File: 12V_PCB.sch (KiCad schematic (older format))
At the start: 8 parts, among them J1 12V IN, J2 RPI CONN, J3 BTN CONN, J4 LED CONN, Q1 PMV40UN2R

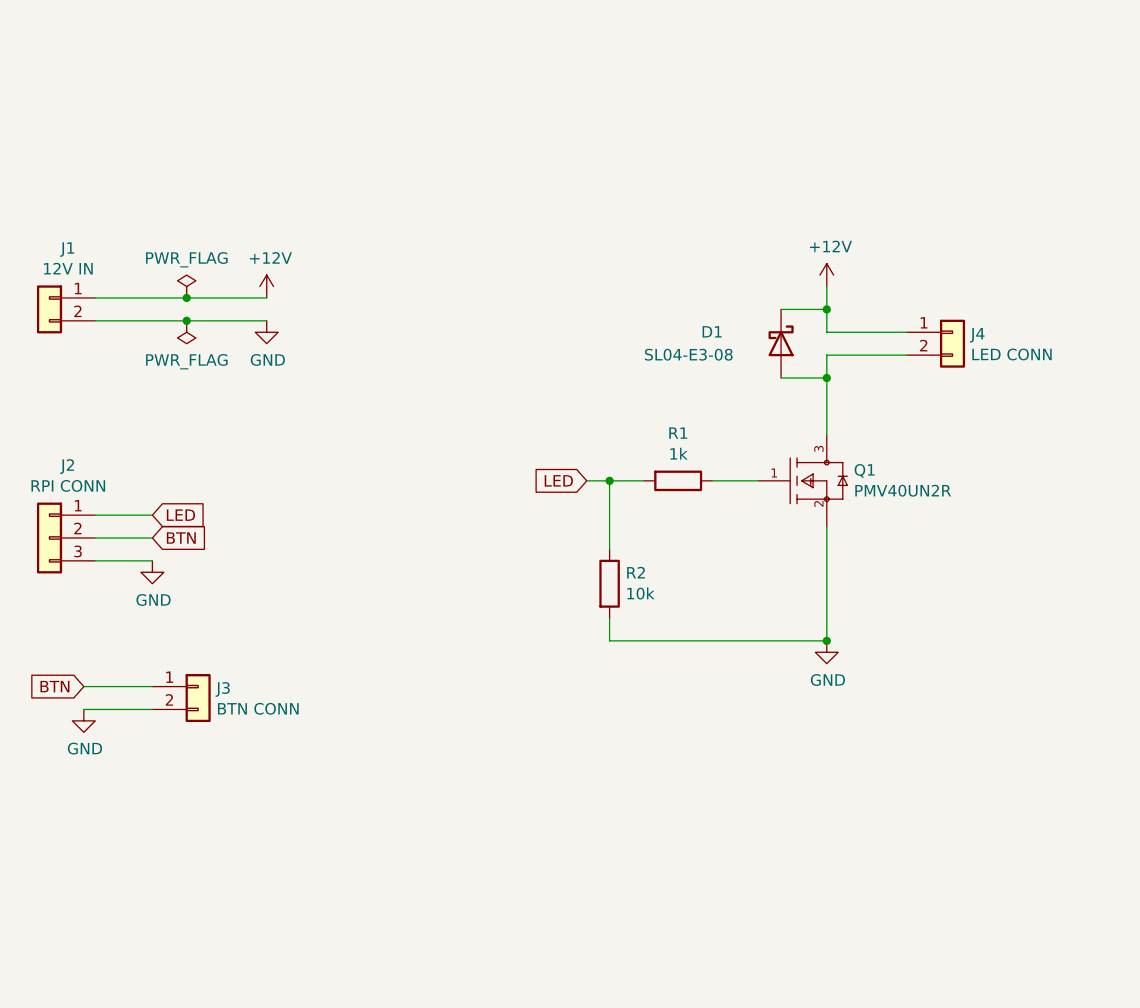
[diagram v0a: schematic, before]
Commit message: added LED_BTN section
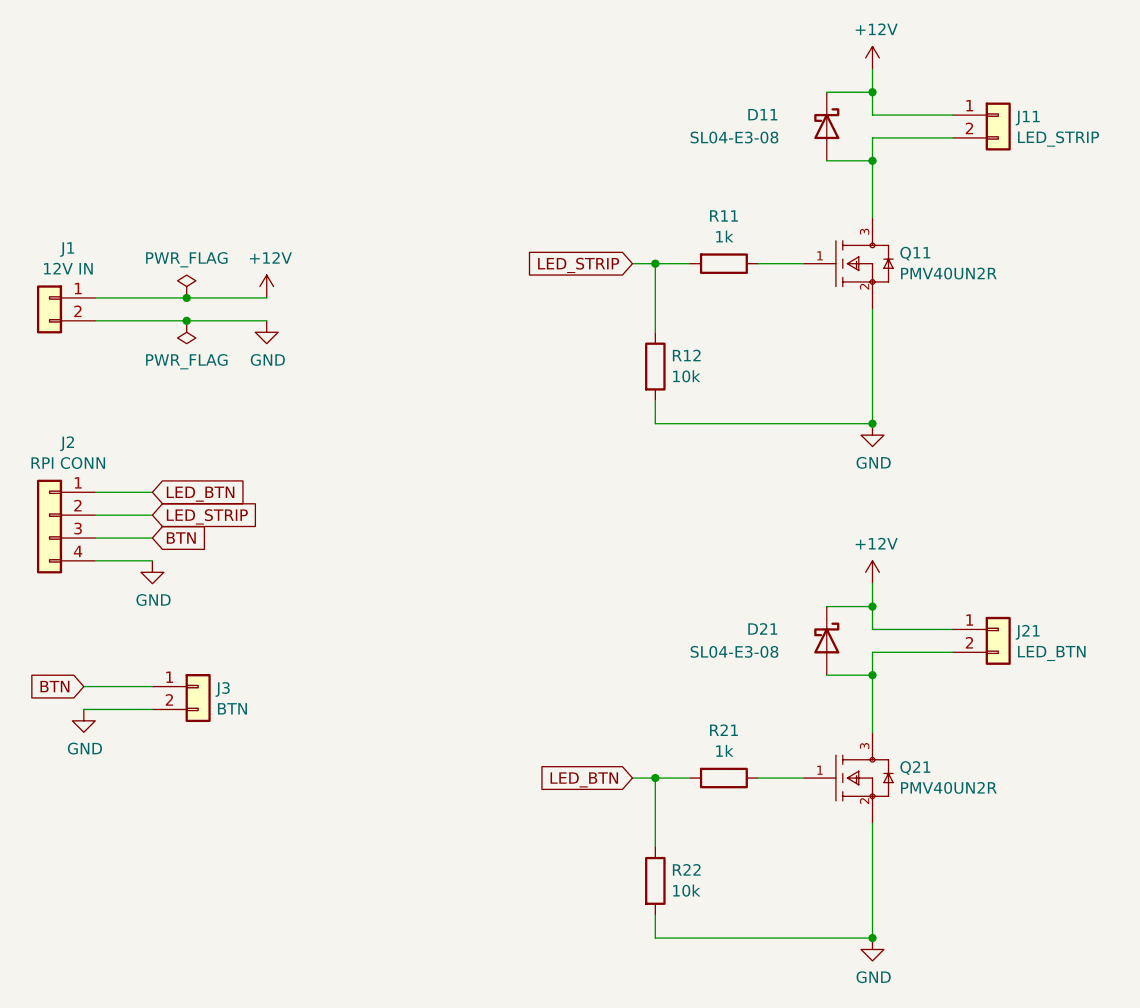
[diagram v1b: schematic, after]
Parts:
- removed J2: RPI CONN, Connector_PinSocket_2.54mm:PinSocket_1x03_P2.54mm_Vertical, symbol Connector_Generic:Conn_01x03
- added D21: SL04-E3-08, Diode_SMD:D_0603_1608Metric_Pad1.05x0.95mm_HandSolder, symbol Device:D_Schottky
- added J2: RPI CONN, Connector_PinSocket_2.54mm:PinSocket_1x04_P2.54mm_Vertical, symbol Connector_Generic:Conn_01x04
- added J21: LED_BTN, Connector_Molex:Molex_KK-254_AE-6410-02A_1x02_P2.54mm_Vertical, symbol Connector_Generic:Conn_01x02
- added Q21: PMV40UN2R, PMV40UN2R:Nexperia-SOT23-01_2018-0-0, symbol PMV40UN2R:PMV40UN2R
- added R21: 1k, Resistor_SMD:R_0603_1608Metric_Pad0.98x0.95mm_HandSolder, symbol Device:R
- added R22: 10k, Resistor_SMD:R_0603_1608Metric_Pad0.98x0.95mm_HandSolder, symbol Device:R
- J11: renamed from J4; value LED CONN -> LED_STRIP
- J3: value BTN CONN -> BTN
- renumbered D1 to D11, Q1 to Q11, R1 to R11, R2 to R12
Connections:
- net +12V: now also D21.1 (K), J21.1 (Pin_1)
- net BTN: now also J2.3 (Pin_3)
- net GND: now also J2.4 (Pin_4), Q21.2 (S), R22.2
- net LED renamed LED_STRIP
- net LED_STRIP: now also J2.2 (Pin_2)
- new net: Q21.1 (G), R21.1
- new net: D21.2 (A), J21.2 (Pin_2), Q21.3 (D)
- new net LED_BTN: J2.1 (Pin_1), R21.2, R22.1
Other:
- moved on the sheet: D11, J11, Q11, R11, R12

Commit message: Final version with panelization
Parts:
- removed D11, D21: SL04-E3-08, Diode_SMD:D_0603_1608Metric_Pad1.05x0.95mm_HandSolder, symbol Device:D_Schottky
- removed Q11, Q21: PMV40UN2R, PMV40UN2R:Nexperia-SOT23-01_2018-0-0, symbol PMV40UN2R:PMV40UN2R
- added Q11, Q21: IRLL2705PBF, Package_TO_SOT_SMD:SOT-223-3_TabPin2, symbol Device:Q_NMOS_GDS
- J1: footprint Connector_BarrelJack:BarrelJack_CUI_PJ-063AH_Horizontal -> Connector_BarrelJack:BarrelJack_Horizontal
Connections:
- net +12V: now also J11.2 (Pin_2), J21.2 (Pin_2); no longer J11.1 (Pin_1), J21.1 (Pin_1)
- net GND: now also Q11.3 (S), Q21.3 (S)
- net at R11.1: now also Q11.1 (G)
- net at R21.1: now also Q21.1 (G)
- new net: J11.1 (Pin_1), Q11.2 (D)
- new net: J21.1 (Pin_1), Q21.2 (D)
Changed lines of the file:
@@
 	7650 1450 7300 1450
 Wire Wire Line
-	7300 1450 7300 1350
-Wire Wire Line
-	7300 1900 7300 1650
-Wire Wire Line
 	7300 1550 7650 1550
-$Comp
-L Device:D_Schottky D11
-U 1 1 626F6136
-P 7100 1500
-F 0 "D11" V 7050 1150 50  0000 L CNN
-F 1 "SL04-E3-08" V 7150 900 50  0000 L CNN
-F 2 "Diode_SMD:D_0603_1608Metric_Pad1.05x0.95mm_HandSolder" H 7100 1500 50  0001 C CNN
-F 3 "~" H 7100 1500 50  0001 C CNN
-	1    7100 1500
-	0    1    1    0
-$EndComp
-$Comp
-L PMV40UN2R:PMV40UN2R Q11
-U 1 1 626FEB6E
-P 6900 2100
-F 0 "Q11" H 7418 2146 50  0000 L CNN
-F 1 "PMV40UN2R" H 7418 2055 50  0000 L CNN
-F 2 "PMV40UN2R:Nexperia-SOT23-01_2018-0-0" H 6900 2600 50  0001 L CNN
-F 3 "https://assets.nexperia.com/documents/data-sheet/PMV40UN2.pdf" H 6900 2700 50  0001 L CNN
-F 4 "+150°C" H 6900 2800 50  0001 L CNN "ambient temperature range high"
-F 5 "-55°C" H 6900 2900 50  0001 L CNN "ambient temperature range low"
-F 6 "Trans" H 6900 3000 50  0001 L CNN "category"
-F 7 "3.7A" H 6900 3100 50  0001 L CNN "continuous drain current"
-F 8 "Discrete Semiconductors" H 6900 3200 50  0001 L CNN "device class L1"
-F 9 "Transistors" H 6900 3300 50  0001 L CNN "device class L2"
-F 10 "MOSFETs" H 6900 3400 50  0001 L CNN "device class L3"
-F 11 "MOSFET N-CH 30V 3.7A SOT23" H 6900 3500 50  0001 L CNN "digikey description"
-F 12 "1727-1900-1-ND" H 6900 3600 50  0001 L CNN "digikey part number"
-F 13 "30V" H 6900 3700 50  0001 L CNN "drain to source breakdown voltage"
-F 14 "36mΩ" H 6900 3800 50  0001 L CNN "drain to source resistance"
-F 15 "30V" H 6900 3900 50  0001 L CNN "drain to source voltage"
-F 16 "https://assets.nexperia.com/documents/outline-drawing/SOT23.pdf" H 6900 4000 50  0001 L CNN "footprint url"
-F 17 "12V" H 6900 4100 50  0001 L CNN "gate to source voltage"
-F 18 "1.1mm" H 6900 4200 50  0001 L CNN "height"
-F 19 "635pF @ 15V" H 6900 4300 50  0001 L CNN "input capacitace at vds"
-F 20 "yes" H 6900 4400 50  0001 L CNN "lead free"
-F 21 "ff33d3c5ec30aaae" H 6900 4500 50  0001 L CNN "library id"
-F 22 "Nexperia" H 6900 4600 50  0001 L CNN "manufacturer"
-F 23 "+150°C" H 6900 4700 50  0001 L CNN "max junction temp"
-F 24 "771-PMV40UN2R" H 6900 4800 50  0001 L CNN "mouser part number"
-F 25 "1" H 6900 4900 50  0001 L CNN "number of N channels"
-F 26 "1" H 6900 5000 50  0001 L CNN "number of channels"
-F 27 "SOT23-3" H 6900 5100 50  0001 L CNN "package"
-F 28 "490mW" H 6900 5200 50  0001 L CNN "power dissipation"
-F 29 "yes" H 6900 5300 50  0001 L CNN "rohs"
-F 30 "MOSFET" H 6900 5400 50  0001 L CNN "technology"
-F 31 "+150°C" H 6900 5500 50  0001 L CNN "temperature range high"
-F 32 "0.4V" H 6900 5600 50  0001 L CNN "threshold vgs"
-F 33 "34ns" H 6900 5700 50  0001 L CNN "turn off delay time"
-F 34 "9ns" H 6900 5800 50  0001 L CNN "turn on delay time"
-	1    6900 2100
-	1    0    0    -1
-$EndComp
-Connection ~ 7300 1650
-Wire Wire Line
-	7300 1650 7300 1550
-Connection ~ 7300 1350
-Wire Wire Line
-	7300 1350 7300 1250
-Wire Wire Line
-	7100 1350 7300 1350
-Wire Wire Line
-	7100 1650 7300 1650
 Wire Wire Line
 	3900 2250 4300 2250
@@
 Connection ~ 4300 2350
 $Comp
-L Connector_Generic:Conn_01x02 J1
-U 1 1 626FA927
-P 3700 2250
-F 0 "J1" H 3618 2467 50  0000 C CNN
-F 1 "12V IN" H 3618 2376 50  0000 C CNN
-F 2 "Connector_BarrelJack:BarrelJack_CUI_PJ-063AH_Horizontal" H 3700 2250 50  0001 C CNN
-F 3 "~" H 3700 2250 50  0001 C CNN
-	1    3700 2250
-	-1   0    0    -1
-$EndComp
-$Comp
 L Connector_Generic:Conn_01x04 J2
 U 1 1 62737001
@@
 	7650 3700 7300 3700
 Wire Wire Line
-	7300 3700 7300 3600
-Wire Wire Line
-	7300 4150 7300 3900
-Wire Wire Line
 	7300 3800 7650 3800
-$Comp
-L Device:D_Schottky D21
-U 1 1 62747927
-P 7100 3750
-F 0 "D21" V 7050 3400 50  0000 L CNN
-F 1 "SL04-E3-08" V 7150 3150 50  0000 L CNN
-F 2 "Diode_SMD:D_0603_1608Metric_Pad1.05x0.95mm_HandSolder" H 7100 3750 50  0001 C CNN
-F 3 "~" H 7100 3750 50  0001 C CNN
-	1    7100 3750
-	0    1    1    0
-$EndComp
-$Comp
-L PMV40UN2R:PMV40UN2R Q21
-U 1 1 6274794C
-P 6900 4350
-F 0 "Q21" H 7418 4396 50  0000 L CNN
-F 1 "PMV40UN2R" H 7418 4305 50  0000 L CNN
-F 2 "PMV40UN2R:Nexperia-SOT23-01_2018-0-0" H 6900 4850 50  0001 L CNN
-F 3 "https://assets.nexperia.com/documents/data-sheet/PMV40UN2.pdf" H 6900 4950 50  0001 L CNN
-F 4 "+150°C" H 6900 5050 50  0001 L CNN "ambient temperature range high"
-F 5 "-55°C" H 6900 5150 50  0001 L CNN "ambient temperature range low"
-F 6 "Trans" H 6900 5250 50  0001 L CNN "category"
-F 7 "3.7A" H 6900 5350 50  0001 L CNN "continuous drain current"
-F 8 "Discrete Semiconductors" H 6900 5450 50  0001 L CNN "device class L1"
-F 9 "Transistors" H 6900 5550 50  0001 L CNN "device class L2"
-F 10 "MOSFETs" H 6900 5650 50  0001 L CNN "device class L3"
-F 11 "MOSFET N-CH 30V 3.7A SOT23" H 6900 5750 50  0001 L CNN "digikey description"
-F 12 "1727-1900-1-ND" H 6900 5850 50  0001 L CNN "digikey part number"
-F 13 "30V" H 6900 5950 50  0001 L CNN "drain to source breakdown voltage"
-F 14 "36mΩ" H 6900 6050 50  0001 L CNN "drain to source resistance"
-F 15 "30V" H 6900 6150 50  0001 L CNN "drain to source voltage"
-F 16 "https://assets.nexperia.com/documents/outline-drawing/SOT23.pdf" H 6900 6250 50  0001 L CNN "footprint url"
-F 17 "12V" H 6900 6350 50  0001 L CNN "gate to source voltage"
-F 18 "1.1mm" H 6900 6450 50  0001 L CNN "height"
-F 19 "635pF @ 15V" H 6900 6550 50  0001 L CNN "input capacitace at vds"
-F 20 "yes" H 6900 6650 50  0001 L CNN "lead free"
-F 21 "ff33d3c5ec30aaae" H 6900 6750 50  0001 L CNN "library id"
-F 22 "Nexperia" H 6900 6850 50  0001 L CNN "manufacturer"
-F 23 "+150°C" H 6900 6950 50  0001 L CNN "max junction temp"
-F 24 "771-PMV40UN2R" H 6900 7050 50  0001 L CNN "mouser part number"
-F 25 "1" H 6900 7150 50  0001 L CNN "number of N channels"
-F 26 "1" H 6900 7250 50  0001 L CNN "number of channels"
-F 27 "SOT23-3" H 6900 7350 50  0001 L CNN "package"
-F 28 "490mW" H 6900 7450 50  0001 L CNN "power dissipation"
-F 29 "yes" H 6900 7550 50  0001 L CNN "rohs"
-F 30 "MOSFET" H 6900 7650 50  0001 L CNN "technology"
-F 31 "+150°C" H 6900 7750 50  0001 L CNN "temperature range high"
-F 32 "0.4V" H 6900 7850 50  0001 L CNN "threshold vgs"
-F 33 "34ns" H 6900 7950 50  0001 L CNN "turn off delay time"
-F 34 "9ns" H 6900 8050 50  0001 L CNN "turn on delay time"
-	1    6900 4350
-	1    0    0    -1
-$EndComp
-Connection ~ 7300 3900
-Wire Wire Line
-	7300 3900 7300 3800
-Connection ~ 7300 3600
-Wire Wire Line
-	7300 3600 7300 3500
-Wire Wire Line
-	7100 3600 7300 3600
-Wire Wire Line
-	7100 3900 7300 3900
 $Comp
 L Connector_Generic:Conn_01x02 J11
 U 1 1 626FCFC4
-P 7850 1450
-F 0 "J11" H 7930 1442 50  0000 L CNN
-F 1 "LED_STRIP" H 7930 1351 50  0000 L CNN
-F 2 "Connector_Molex:Molex_KK-254_AE-6410-02A_1x02_P2.54mm_Vertical" H 7850 1450 50  0001 C CNN
-F 3 "~" H 7850 1450 50  0001 C CNN
-	1    7850 1450
-	1    0    0    -1
+P 7850 1550
+F 0 "J11" H 7930 1542 50  0000 L CNN
+F 1 "LED_STRIP" H 7930 1451 50  0000 L CNN
+F 2 "Connector_Molex:Molex_KK-254_AE-6410-02A_1x02_P2.54mm_Vertical" H 7850 1550 50  0001 C CNN
+F 3 "~" H 7850 1550 50  0001 C CNN
+	1    7850 1550
+	1    0    0    1
 $EndComp
 $Comp
 L Connector_Generic:Conn_01x02 J21
 U 1 1 62747958
-P 7850 3700
-F 0 "J21" H 7930 3692 50  0000 L CNN
-F 1 "LED_BTN" H 7930 3601 50  0000 L CNN
-F 2 "Connector_Molex:Molex_KK-254_AE-6410-02A_1x02_P2.54mm_Vertical" H 7850 3700 50  0001 C CNN
-F 3 "~" H 7850 3700 50  0001 C CNN
-	1    7850 3700
-	1    0    0    -1
+P 7850 3800
+F 0 "J21" H 7930 3792 50  0000 L CNN
+F 1 "LED_BTN" H 7930 3701 50  0000 L CNN
+F 2 "Connector_Molex:Molex_KK-254_AE-6410-02A_1x02_P2.54mm_Vertical" H 7850 3800 50  0001 C CNN
+F 3 "~" H 7850 3800 50  0001 C CNN
+	1    7850 3800
+	1    0    0    1
 $EndComp
 $Comp
@@
 	1    0    0    -1
 $EndComp
+Wire Wire Line
+	7300 3800 7300 4150
+Wire Wire Line
+	7300 3500 7300 3700
+Wire Wire Line
+	7300 1250 7300 1450
+Wire Wire Line
+	7300 1550 7300 1900
+$Comp
+L Device:Q_NMOS_GDS Q11
+U 1 1 62760132
+P 7200 2100
+F 0 "Q11" H 7404 2146 50  0000 L CNN
+F 1 "IRLL2705PBF" H 7404 2055 50  0000 L CNN
+F 2 "Package_TO_SOT_SMD:SOT-223-3_TabPin2" H 7400 2200 50  0001 C CNN
+F 3 "~" H 7200 2100 50  0001 C CNN
+	1    7200 2100
+	1    0    0    -1
+$EndComp
+$Comp
+L Device:Q_NMOS_GDS Q21
+U 1 1 62762F3F
+P 7200 4350
+F 0 "Q21" H 7404 4396 50  0000 L CNN
+F 1 "IRLL2705PBF" H 7404 4305 50  0000 L CNN
+F 2 "Package_TO_SOT_SMD:SOT-223-3_TabPin2" H 7400 4450 50  0001 C CNN
+F 3 "~" H 7200 4350 50  0001 C CNN
+	1    7200 4350
+	1    0    0    -1
+$EndComp
+$Comp
+L Connector_Generic:Conn_01x02 J1
+U 1 1 626FA927
+P 3700 2250
+F 0 "J1" H 3618 2467 50  0000 C CNN
+F 1 "12V IN" H 3618 2376 50  0000 C CNN
+F 2 "Connector_BarrelJack:BarrelJack_Horizontal" H 3700 2250 50  0001 C CNN
+F 3 "~" H 3700 2250 50  0001 C CNN
+	1    3700 2250
+	-1   0    0    -1
+$EndComp
 $EndSCHEMATC
